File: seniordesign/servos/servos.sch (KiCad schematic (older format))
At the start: 20 parts, among them CON1 USB-MICRO-B, P1 SERVO_PWMS, U1 FT234XD, U2 MSP430G2153, U3 ADP151AUJZ-3.3-R7, U4 SN74LV1T04, U5 SN74LV1T04, U6 SN74LV1T04, U7 SN74LV1T04

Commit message: Working servos schematic; can generate footprints!
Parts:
- P1: footprint Wire_Pads:SolderWirePad_4xInline_1mmDrill -> Pin_Headers:Pin_Header_Straight_1x04
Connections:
- wire segments 101 -> 100
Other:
- moved on the sheet: R3
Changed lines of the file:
@@
 LIBS:FERRITEBEAD
 LIBS:servos-cache
-EELAYER 27 0
+EELAYER 25 0
 EELAYER END
 $Descr User 7087 9449
@@
 $EndComp
 $Comp
-L +5V #PWR6
+L +5V #PWR01
 U 1 1 553840C0
 P 2100 3600
-F 0 "#PWR6" H 2100 3450 50  0001 C CNN
+F 0 "#PWR01" H 2100 3450 50  0001 C CNN
 F 1 "+5V" H 2100 3740 50  0000 C CNN
 F 2 "" H 2100 3600 60  0000 C CNN
@@
 $EndComp
 $Comp
-L GND #PWR3
+L GND #PWR02
 U 1 1 553840E4
 P 1200 1450
-F 0 "#PWR3" H 1200 1200 50  0001 C CNN
+F 0 "#PWR02" H 1200 1200 50  0001 C CNN
 F 1 "GND" H 1200 1300 50  0000 C CNN
 F 2 "" H 1200 1450 60  0000 C CNN
@@
 $EndComp
 $Comp
-L GND #PWR7
+L GND #PWR03
 U 1 1 55384126
 P 2400 1450
-F 0 "#PWR7" H 2400 1200 50  0001 C CNN
+F 0 "#PWR03" H 2400 1200 50  0001 C CNN
 F 1 "GND" H 2400 1300 50  0000 C CNN
 F 2 "" H 2400 1450 60  0000 C CNN
@@
 $EndComp
 $Comp
-L GND #PWR9
+L GND #PWR04
 U 1 1 55384546
 P 3150 1600
-F 0 "#PWR9" H 3150 1350 50  0001 C CNN
+F 0 "#PWR04" H 3150 1350 50  0001 C CNN
 F 1 "GND" H 3150 1450 50  0000 C CNN
 F 2 "" H 3150 1600 60  0000 C CNN
@@
 $EndComp
 $Comp
-L GND #PWR8
+L GND #PWR05
 U 1 1 55384681
 P 2600 1500
-F 0 "#PWR8" H 2600 1250 50  0001 C CNN
+F 0 "#PWR05" H 2600 1250 50  0001 C CNN
 F 1 "GND" H 2600 1350 50  0000 C CNN
 F 2 "" H 2600 1500 60  0000 C CNN
@@
 $EndComp
 $Comp
-L GND #PWR15
+L GND #PWR06
 U 1 1 5538469E
 P 4300 1750
-F 0 "#PWR15" H 4300 1500 50  0001 C CNN
+F 0 "#PWR06" H 4300 1500 50  0001 C CNN
 F 1 "GND" H 4300 1600 50  0000 C CNN
 F 2 "" H 4300 1750 60  0000 C CNN
@@
 $EndComp
 $Comp
-L +5V #PWR1
+L +5V #PWR07
 U 1 1 55384F0E
 P 650 750
-F 0 "#PWR1" H 650 600 50  0001 C CNN
+F 0 "#PWR07" H 650 600 50  0001 C CNN
 F 1 "+5V" H 650 890 50  0000 C CNN
 F 2 "" H 650 750 60  0000 C CNN
@@
 $EndComp
 $Comp
-L GND #PWR13
+L GND #PWR08
 U 1 1 55385791
 P 3500 5050
-F 0 "#PWR13" H 3500 4800 50  0001 C CNN
+F 0 "#PWR08" H 3500 4800 50  0001 C CNN
 F 1 "GND" H 3500 4900 50  0000 C CNN
 F 2 "" H 3500 5050 60  0000 C CNN
@@
 $EndComp
 $Comp
-L GND #PWR2
+L GND #PWR09
 U 1 1 553858B7
 P 950 4700
-F 0 "#PWR2" H 950 4450 50  0001 C CNN
+F 0 "#PWR09" H 950 4450 50  0001 C CNN
 F 1 "GND" H 950 4550 50  0000 C CNN
 F 2 "" H 950 4700 60  0000 C CNN
@@
 $EndComp
 $Comp
-L GND #PWR5
+L GND #PWR010
 U 1 1 5538599B
 P 2000 5200
-F 0 "#PWR5" H 2000 4950 50  0001 C CNN
+F 0 "#PWR010" H 2000 4950 50  0001 C CNN
 F 1 "GND" H 2000 5050 50  0000 C CNN
 F 2 "" H 2000 5200 60  0000 C CNN
@@
 $EndComp
 $Comp
-L GND #PWR10
+L GND #PWR011
 U 1 1 55386487
 P 3150 3900
-F 0 "#PWR10" H 3150 3650 50  0001 C CNN
+F 0 "#PWR011" H 3150 3650 50  0001 C CNN
 F 1 "GND" H 3150 3750 50  0000 C CNN
 F 2 "" H 3150 3900 60  0000 C CNN
@@
 $EndComp
 $Comp
-L GND #PWR11
+L GND #PWR012
 U 1 1 553864AB
 P 3400 3900
-F 0 "#PWR11" H 3400 3650 50  0001 C CNN
+F 0 "#PWR012" H 3400 3650 50  0001 C CNN
 F 1 "GND" H 3400 3750 50  0000 C CNN
 F 2 "" H 3400 3900 60  0000 C CNN
@@
 $EndComp
 $Comp
-L GND #PWR16
+L GND #PWR013
 U 1 1 55386574
 P 4350 3550
-F 0 "#PWR16" H 4350 3300 50  0001 C CNN
+F 0 "#PWR013" H 4350 3300 50  0001 C CNN
 F 1 "GND" H 4350 3400 50  0000 C CNN
 F 2 "" H 4350 3550 60  0000 C CNN
@@
 $EndComp
 $Comp
-L +5V #PWR12
+L +5V #PWR014
 U 1 1 55386FD7
-P 3500 4200
-F 0 "#PWR12" H 3500 4050 50  0001 C CNN
-F 1 "+5V" H 3500 4340 50  0000 C CNN
-F 2 "" H 3500 4200 60  0000 C CNN
-F 3 "" H 3500 4200 60  0000 C CNN
-	1    3500 4200
+P 3500 4050
+F 0 "#PWR014" H 3500 3900 50  0001 C CNN
+F 1 "+5V" H 3500 4190 50  0000 C CNN
+F 2 "" H 3500 4050 60  0000 C CNN
+F 3 "" H 3500 4050 60  0000 C CNN
+	1    3500 4050
 	1    0    0    -1
 $EndComp
@@
 L R R3
 U 1 1 55387053
-P 3500 4400
-F 0 "R3" V 3580 4400 50  0000 C CNN
-F 1 "10k" V 3500 4400 50  0000 C CNN
-F 2 "Resistors_SMD:R_0805" V 3430 4400 30  0001 C CNN
-F 3 "" H 3500 4400 30  0000 C CNN
-	1    3500 4400
-	1    0    0    -1
-$EndComp
-$Comp
-L GND #PWR18
+P 3500 4300
+F 0 "R3" V 3580 4300 50  0000 C CNN
+F 1 "10k" V 3500 4300 50  0000 C CNN
+F 2 "Resistors_SMD:R_0805" V 3430 4300 30  0001 C CNN
+F 3 "" H 3500 4300 30  0000 C CNN
+	1    3500 4300
+	1    0    0    -1
+$EndComp
+$Comp
+L GND #PWR015
 U 1 1 55389491
 P 5700 6950
-F 0 "#PWR18" H 5700 6700 50  0001 C CNN
+F 0 "#PWR015" H 5700 6700 50  0001 C CNN
 F 1 "GND" H 5700 6800 50  0000 C CNN
 F 2 "" H 5700 6950 60  0000 C CNN
@@
 $EndComp
 $Comp
-L +5V #PWR14
+L +5V #PWR016
 U 1 1 55389B48
 P 4200 4100
-F 0 "#PWR14" H 4200 3950 50  0001 C CNN
+F 0 "#PWR016" H 4200 3950 50  0001 C CNN
 F 1 "+5V" H 4200 4240 50  0000 C CNN
 F 2 "" H 4200 4100 60  0000 C CNN
@@
 F 0 "P1" H 3250 5850 50  0000 C CNN
 F 1 "SERVO_PWMS" V 3350 5600 50  0000 C CNN
-F 2 "Wire_Pads:SolderWirePad_4xInline_1mmDrill" H 3250 5600 60  0001 C CNN
+F 2 "Pin_Headers:Pin_Header_Straight_1x04" H 3250 5600 60  0001 C CNN
 F 3 "" H 3250 5600 60  0000 C CNN
 	1    3250 5600
@@
 $EndComp
 $Comp
-L GND #PWR17
+L GND #PWR017
 U 1 1 55394012
 P 4600 1750
-F 0 "#PWR17" H 4600 1500 50  0001 C CNN
+F 0 "#PWR017" H 4600 1500 50  0001 C CNN
 F 1 "GND" H 4600 1600 50  0000 C CNN
 F 2 "" H 4600 1750 60  0000 C CNN
@@
 	2950 4300 2950 3450
 Wire Wire Line
-	1700 3450 3150 3450
+	1800 3450 3150 3450
 Wire Wire Line
 	3000 4400 3000 3300
 Wire Wire Line
-	1700 3300 3400 3300
-Wire Wire Line
-	1400 3450 850  3450
-Wire Wire Line
 	850  3450 850  1050
 Wire Wire Line
 	800  1150 800  3300
-Wire Wire Line
-	800  3300 1400 3300
 Wire Wire Line
 	1650 2450 750  2450
@@
 Wire Wire Line
 	3500 4600 2800 4600
-Wire Wire Line
-	3500 4250 3500 4200
 Connection ~ 3500 4600
 Wire Wire Line
@@
 	5650 2450 5200 2450
 Wire Wire Line
-	5350 6700 5700 6700
+	5700 6700 5350 6700
 Wire Wire Line
 	5700 4500 5700 6950
@@
 $EndComp
 $Comp
-L GND #PWR4
+L GND #PWR018
 U 1 1 5539468C
 P 1700 3900
-F 0 "#PWR4" H 1700 3650 50  0001 C CNN
+F 0 "#PWR018" H 1700 3650 50  0001 C CNN
 F 1 "GND" H 1700 3750 50  0000 C CNN
 F 2 "" H 1700 3900 60  0000 C CNN
@@
 Wire Wire Line
 	1700 3850 1700 3900
+Wire Wire Line
+	800  3300 1300 3300
+Wire Wire Line
+	850  3450 1300 3450
+Wire Wire Line
+	1800 3300 3400 3300
 $EndSCHEMATC

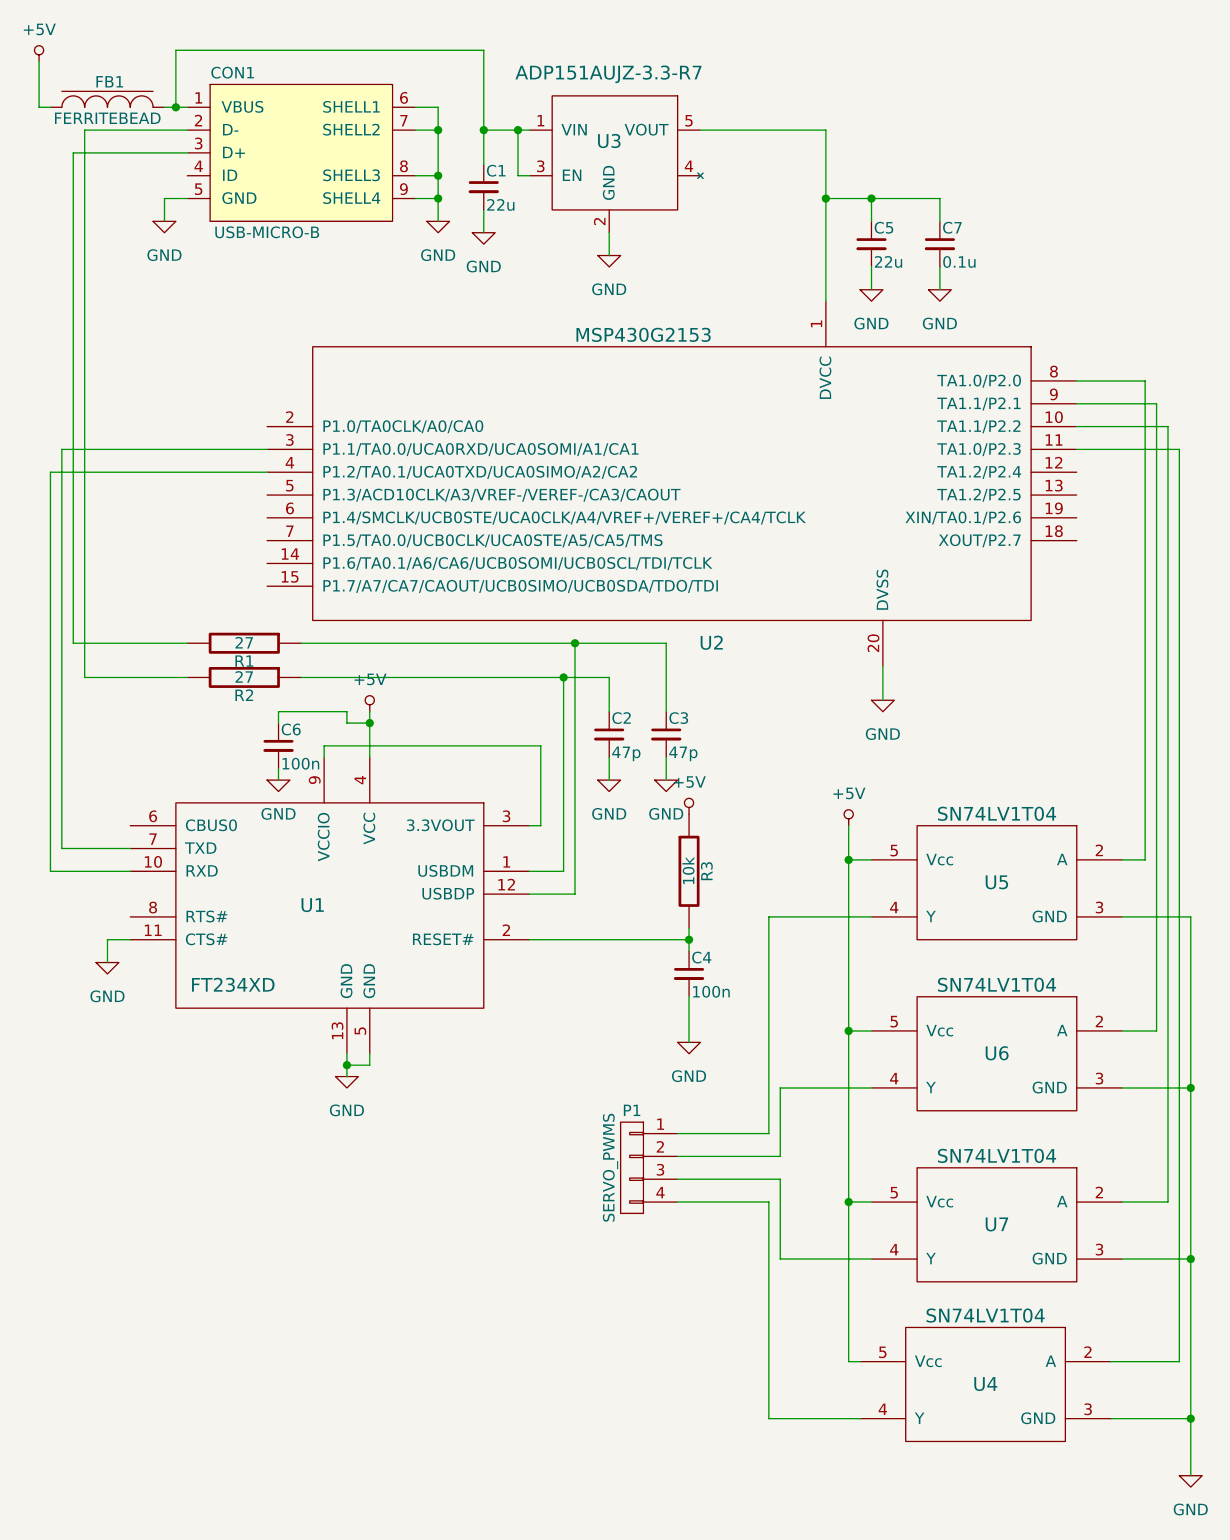
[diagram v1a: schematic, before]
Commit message: Fix servo stuff, regenerate Gerber files for everything
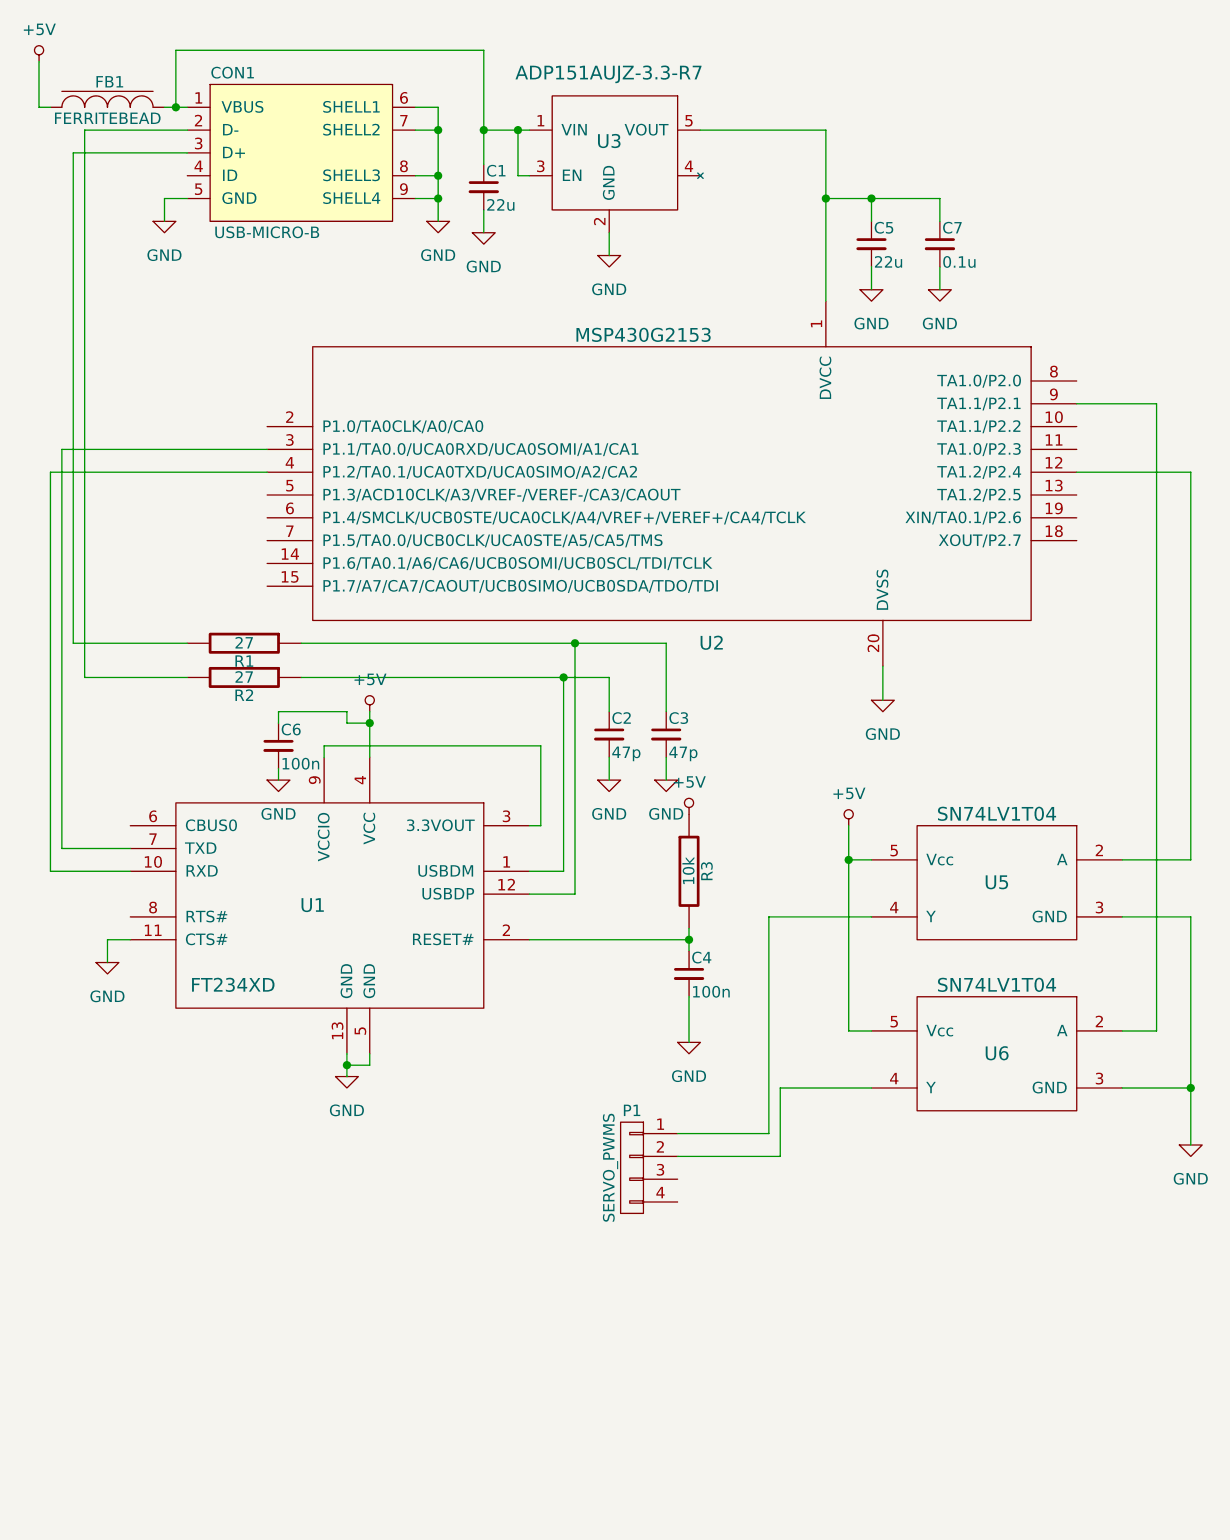
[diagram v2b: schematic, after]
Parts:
- removed U4, U7: SN74LV1T04, Transistors_SMD:sc70-5, symbol SN74LV1T04
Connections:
- net at U5.2 (A): now also U2.12 (TA1.2/P2.4); no longer U2.8 (TA1.0/P2.0)
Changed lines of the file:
@@
-$EndComp
-$Comp
-L SN74LV1T04 U4
-U 1 1 55383CD4
-P 4800 6550
-F 0 "U4" H 4800 6550 60  0000 C CNN
-F 1 "SN74LV1T04" H 4800 6850 60  0000 C CNN
-F 2 "Transistors_SMD:sc70-5" H 4800 6550 60  0001 C CNN
-F 3 "" H 4800 6550 60  0000 C CNN
-	1    4800 6550
-	-1   0    0    -1
 $EndComp
 $Comp
@@
 $EndComp
 $Comp
-L SN74LV1T04 U7
-U 1 1 55383EB7
-P 4850 5850
-F 0 "U7" H 4850 5850 60  0000 C CNN
-F 1 "SN74LV1T04" H 4850 6150 60  0000 C CNN
-F 2 "Transistors_SMD:sc70-5" H 4850 5850 60  0001 C CNN
-F 3 "" H 4850 5850 60  0000 C CNN
-	1    4850 5850
-	-1   0    0    -1
-$EndComp
-$Comp
 L ADP151AUJZ-3.3-R7 U3
 U 1 1 55383F31
@@
 L GND #PWR015
 U 1 1 55389491
-P 5700 6950
-F 0 "#PWR015" H 5700 6700 50  0001 C CNN
-F 1 "GND" H 5700 6800 50  0000 C CNN
-F 2 "" H 5700 6950 60  0000 C CNN
-F 3 "" H 5700 6950 60  0000 C CNN
-	1    5700 6950
+P 5700 5500
+F 0 "#PWR015" H 5700 5250 50  0001 C CNN
+F 1 "GND" H 5700 5350 50  0000 C CNN
+F 2 "" H 5700 5500 60  0000 C CNN
+F 3 "" H 5700 5500 60  0000 C CNN
+	1    5700 5500
 	1    0    0    -1
 $EndComp
@@
 Connection ~ 3500 4600
 Wire Wire Line
-	5200 2150 5500 2150
-Wire Wire Line
-	5500 2150 5500 4250
-Wire Wire Line
-	5500 4250 5400 4250
+	5400 4250 5700 4250
 Wire Wire Line
 	5200 2250 5550 2250
@@
 	5550 5000 5400 5000
 Wire Wire Line
-	5200 2350 5600 2350
-Wire Wire Line
-	5600 2350 5600 5750
-Wire Wire Line
-	5600 5750 5400 5750
-Wire Wire Line
-	5350 6450 5650 6450
-Wire Wire Line
-	5650 6450 5650 2450
-Wire Wire Line
-	5650 2450 5200 2450
-Wire Wire Line
-	5700 6700 5350 6700
-Wire Wire Line
-	5700 4500 5700 6950
-Wire Wire Line
-	5400 6000 5700 6000
-Connection ~ 5700 6700
-Wire Wire Line
-	5400 5250 5700 5250
-Connection ~ 5700 6000
-Wire Wire Line
-	5400 4500 5700 4500
-Connection ~ 5700 5250
-Wire Wire Line
-	4200 4100 4200 6450
+	5700 5250 5400 5250
+Wire Wire Line
+	5700 4500 5400 4500
 Wire Wire Line
 	4200 4250 4300 4250
@@
 Connection ~ 4200 4250
 Wire Wire Line
-	4200 5750 4300 5750
-Connection ~ 4200 5000
-Wire Wire Line
-	4200 6450 4250 6450
-Connection ~ 4200 5750
-Wire Wire Line
 	4300 4500 3850 4500
 Wire Wire Line
@@
 Wire Wire Line
 	3900 5250 4300 5250
-Wire Wire Line
-	4300 6000 3900 6000
-Wire Wire Line
-	3900 6000 3900 5650
-Wire Wire Line
-	3900 5650 3450 5650
-Wire Wire Line
-	3450 5750 3850 5750
-Wire Wire Line
-	3850 5750 3850 6700
-Wire Wire Line
-	3850 6700 4250 6700
 Wire Wire Line
 	1250 950  1250 700
@@
 Wire Wire Line
 	1800 3300 3400 3300
+Wire Wire Line
+	5200 2550 5700 2550
+Wire Wire Line
+	4200 4100 4200 5000
+Connection ~ 5700 5250
+Wire Wire Line
+	5700 4500 5700 5500
+Wire Wire Line
+	5700 2550 5700 4250
 $EndSCHEMATC
